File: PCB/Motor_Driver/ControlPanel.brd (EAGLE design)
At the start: 41.9 x 47.9 mm, 17 parts, among them IC1 L298, X1 22-23-2021, X2 22-23-2021

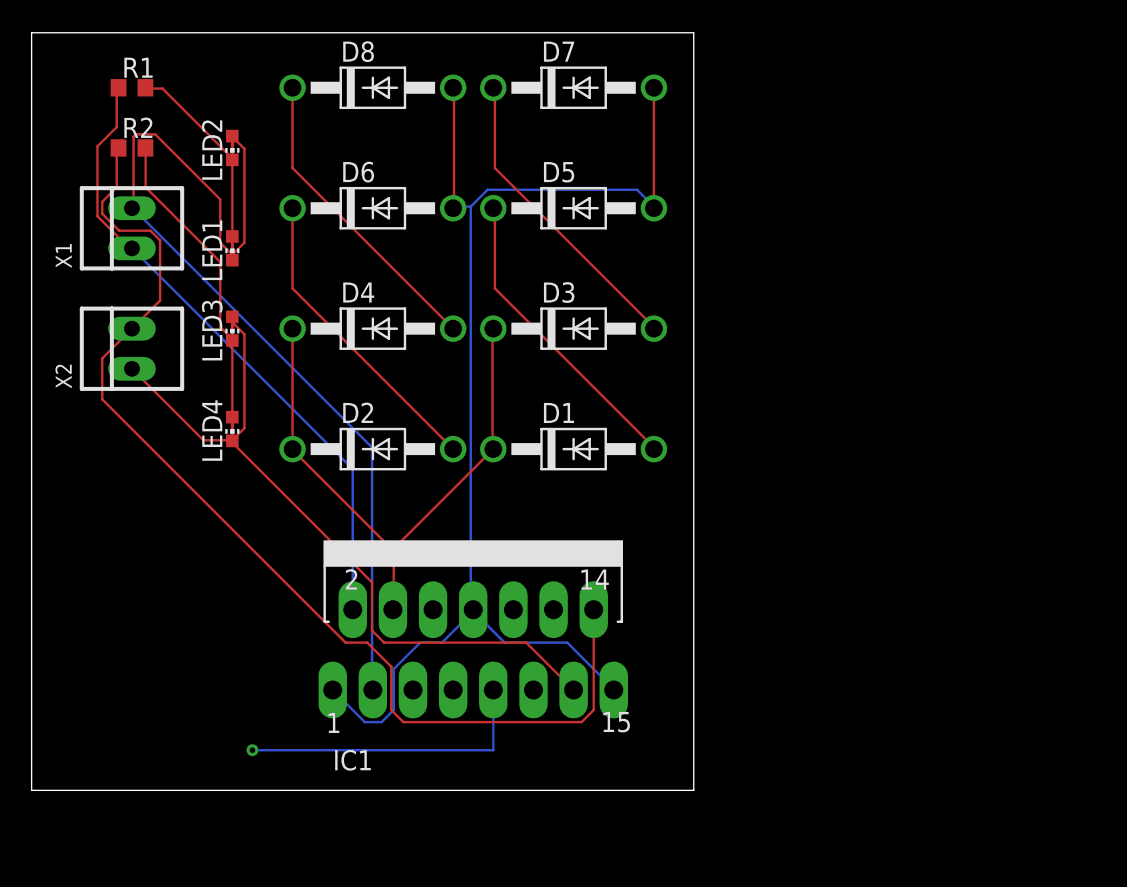
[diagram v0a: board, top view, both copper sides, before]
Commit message: Updated the control PCBA design
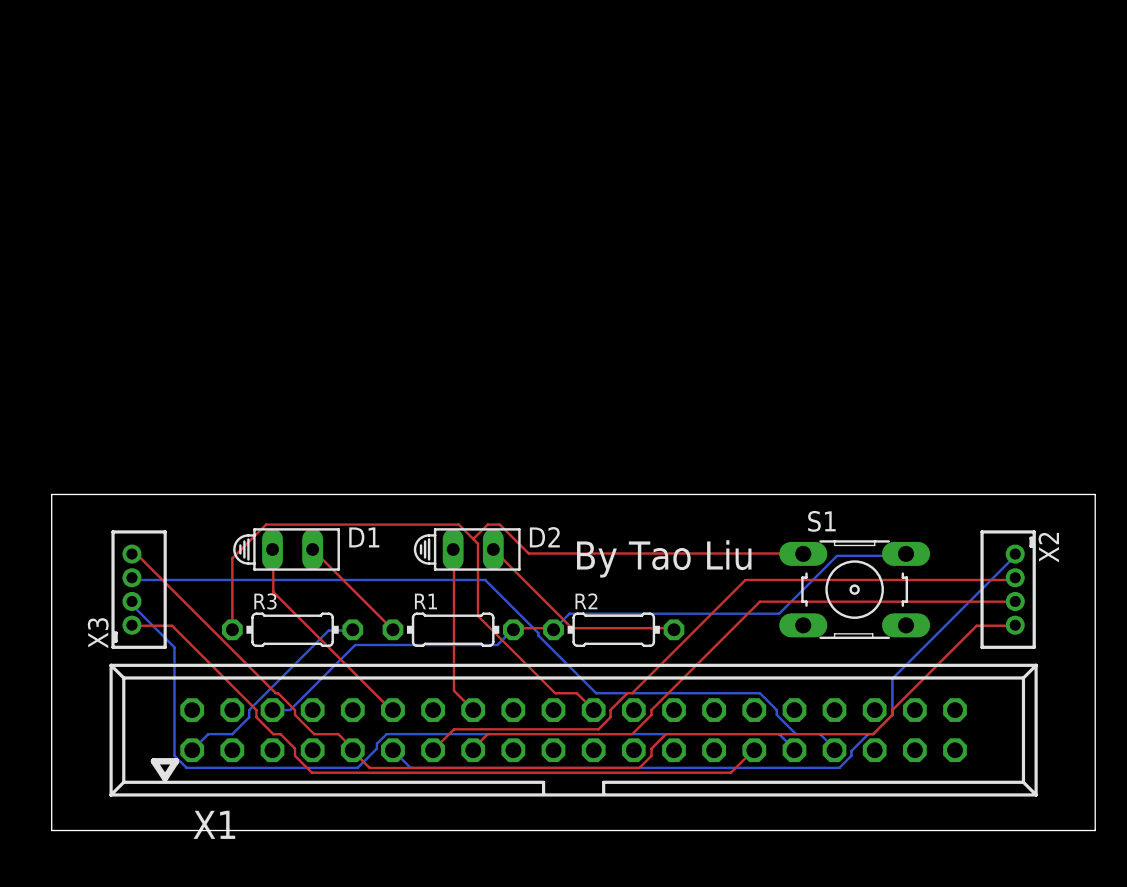
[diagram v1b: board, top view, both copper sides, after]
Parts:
- removed D3, D4, D5, D6, D7, D8: 1N4004, diode:DO41-10
- removed IC1: L298, st-microelectronics:MULTIWATT-15
- removed LED1, LED2, LED3, LED4: (no value), led:CHIP-LED0603
- added R3: (no value), rcl:0204/7
- added S1: (no value), switch-omron:B3F-10XX
- added X3: B4B-ZR, con-jst:B4B-ZR
- D1, D2: value 1N4004 -> HLMP6; device diode:DO41-10 -> display-hp:HLMP6
- R1, R2: device rcl:R0603 -> rcl:0204/7
- X1: value 22-23-2021 -> 057-040-1; device con-molex:22-23-2021 -> con-panduit:057-040-1
- X2: value 22-23-2021 -> B4B-ZR; device con-molex:22-23-2021 -> con-jst:B4B-ZR
- moved X2 57.9 mm to (61.0, 15.2), turned to 270 degrees
- moved R2 43.1 mm to (35.6, 12.7)
- moved X1 42.3 mm to (33.0, 6.35), turned to 0 degrees
- moved R1 39.9 mm to (25.4, 12.7)
- moved D1 18.9 mm to (15.2, 17.8)
- moved D2 8.98 mm to (26.7, 17.8)
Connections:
- removed net ENA: IC1.6
- removed net ENB: IC1.11
- removed net GND: D5.A, D6.A, D7.A, D8.A, IC1.1, IC1.15, IC1.8
- removed net IN1: IC1.5
- removed net IN2: IC1.7
- removed net IN3: IC1.10
- removed net IN4: IC1.12
- removed net N$16: IC1.13, LED3.C, LED4.A, X2.1
- removed net N$9: D3.A, D7.C
- removed net VCC: IC1.9
- new net N$1: D1.A, X1.12
- new net N$2: D2.A, X1.16
- new net N$3: D1.K, R1.1
- new net N$4: R1.2, R2.1, S1.2, X1.6
- new net N$5: D2.K, R2.2
- net N$10: now also X1.11, X2.1; no longer D4.A, D8.C
- net N$11: now also X1.13, X2.2; no longer IC1.2, R1.1, X1.1
- net N$12: now also X1.15, X2.3; no longer LED1.C, LED2.A, R1.2
- net N$13: now also X1.29, X3.1; no longer IC1.3, LED1.A, LED2.C, X1.2
- net N$14: now also X1.31, X3.2; no longer LED3.A, LED4.C, R2.2
- net N$15: now also X1.33, X3.3; no longer IC1.14, R2.1, X2.2
- net N$6: now also R3.2, X1.1; no longer D1.C, D2.C, D3.C, D4.C, IC1.4
- net N$7: now also R3.1, S1.1, X1.22; no longer D1.A, D5.C
- net N$8: now also X1.9, X2.4, X3.4; no longer D2.A, D6.C
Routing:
- net GND: track 79.8 -> 0.00 mm
- net N$16: track 50.4 -> 0.00 mm
- net N$8: track 19.4 -> 66.0 mm
- net N$4: track 0.00 -> 44.3 mm
- net N$7: track 19.5 -> 57.8 mm
- net N$14: track 23.6 -> 52.0 mm
- net N$10: track 19.4 -> 47.0 mm
- net N$6: track 37.2 -> 13.6 mm
- net N$12: track 16.6 -> 38.4 mm
- net N$13: track 64.6 -> 44.3 mm
- net N$9: track 19.5 -> 0.00 mm
- net N$15: track 68.4 -> 49.3 mm
- net VCC: track 19.1 -> 0.00 mm, vias 1 -> 0
- net N$5: track 0.00 -> 13.6 mm
- net N$1: track 0.00 -> 13.4 mm
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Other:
- board size 41.9 x 47.9 mm -> 66 x 21.3 mm
- board text added: "By Tao Liu"
